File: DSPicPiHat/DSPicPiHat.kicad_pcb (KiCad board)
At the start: 2 copper layers, 65 x 66.5 mm, 82 parts, among them J1 Conn_01x09_Female, J4 Conn_PIC_ICSP_ICD, J5 USB_C_Receptacle_USB2.0, J6 PowerInput, J8 RasPiHeaders, SW1 POWER_Select, SW2 SW_DIP_x08, U1 DSPIC33CH512MP508T-I_PT, U10 DF5A6.2CJE_LM, U11 FT230XS, U12 NCP1117-3.3_SOT223, U3 DF5A6.2CJE_LM, U4 DF5A6.2CJE_LM, U6 DF5A6.2CJE_LM, U7 DF5A6.2CJE_LM, U9 DF5A6.2CJE_LM, Y1 16MHz

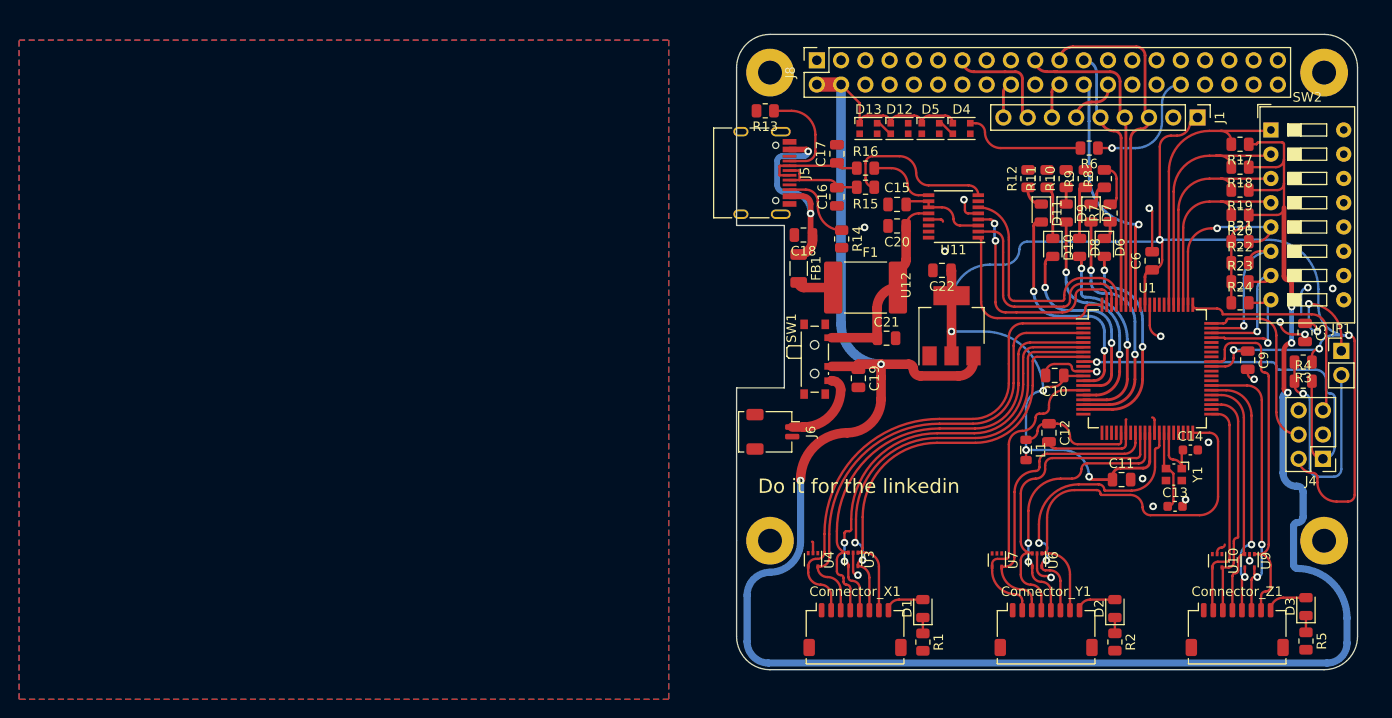
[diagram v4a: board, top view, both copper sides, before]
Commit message: added fiducials and slightly moved some things around.
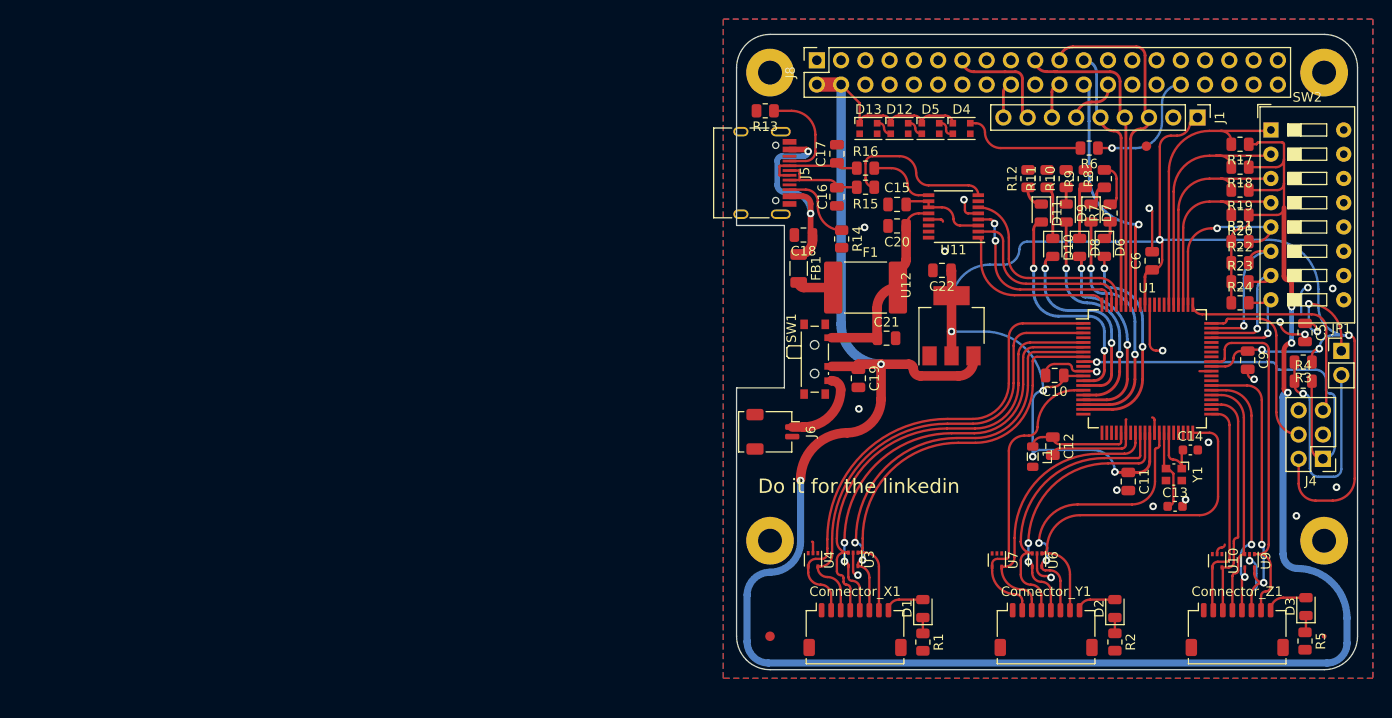
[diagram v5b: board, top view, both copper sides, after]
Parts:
- added REF**: Fiducial_0.5mm_Mask1.5mm, Fiducial:Fiducial_0.5mm_Mask1.5mm, F.Cu at (118.0, 136.5)
- added REF**: Fiducial_1mm_Mask2mm, Fiducial:Fiducial_1mm_Mask2mm, F.Cu at (60.0, 136.5)
- added REF**: Fiducial_1mm_Mask2mm, Fiducial:Fiducial_1mm_Mask2mm, F.Cu at (99.4, 85.2)
- moved C12 1.46 mm to (89.6, 116.6)
- moved L1 0.99 mm to (87.5, 117.7)
- moved C11 0.73 mm to (97.5, 120.3), turned to -90 degrees
- moved R5 0.10 mm to (116.0, 137.0)
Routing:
- net AVSS: track 54.8 -> 61.1 mm, vias 18 -> 21
- net U1RX: track 25.2 -> 20.7 mm
- net U1CTS: track 25.9 -> 21.4 mm
- net U1RTS: track 24.0 -> 19.5 mm
- net EXT_ADC_Y_03: track 42.7 -> 38.4 mm
- net U1TX: track 21.2 -> 17.7 mm
- net VDD: track 177.2 -> 173.8 mm
- net EXT_Y_PWM_01: track 31.6 -> 29.1 mm
- net EXT_ADC_Y_00: track 32.0 -> 29.5 mm
- net Net-(D12-Pad4): track 0.00 -> 2.00 mm
- net AVDD: track 13.0 -> 11.3 mm
- net EXT_ADC_Y_01: track 29.4 -> 27.8 mm
- net +5V: track 254.2 -> 253.1 mm
- net DIP_07: track 13.4 -> 12.3 mm
- net EXT_ADC_X_03: track 44.7 -> 43.7 mm
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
